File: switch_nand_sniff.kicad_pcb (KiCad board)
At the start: 2 copper layers, 35.4 x 28.8 mm, 3 parts, among them P1 CONN_02X15, P2 CONN_02X15

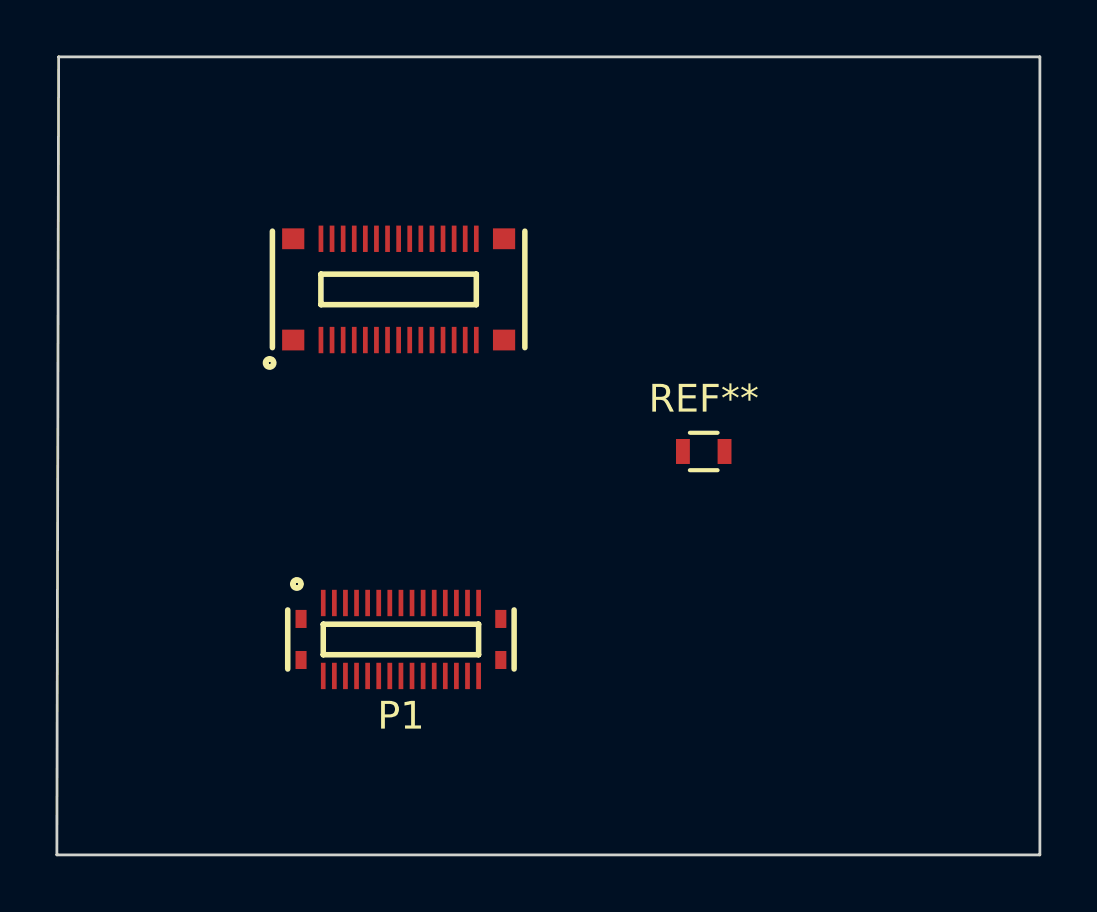
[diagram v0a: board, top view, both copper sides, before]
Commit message: Improved stencil design for manufacturing *removed resistor stencil because tbh why was it there in the first place *shrunk pad size to decrease risk of shorts when using solder paste *moved pads to edge of stencils to improve rate of manufacturing.
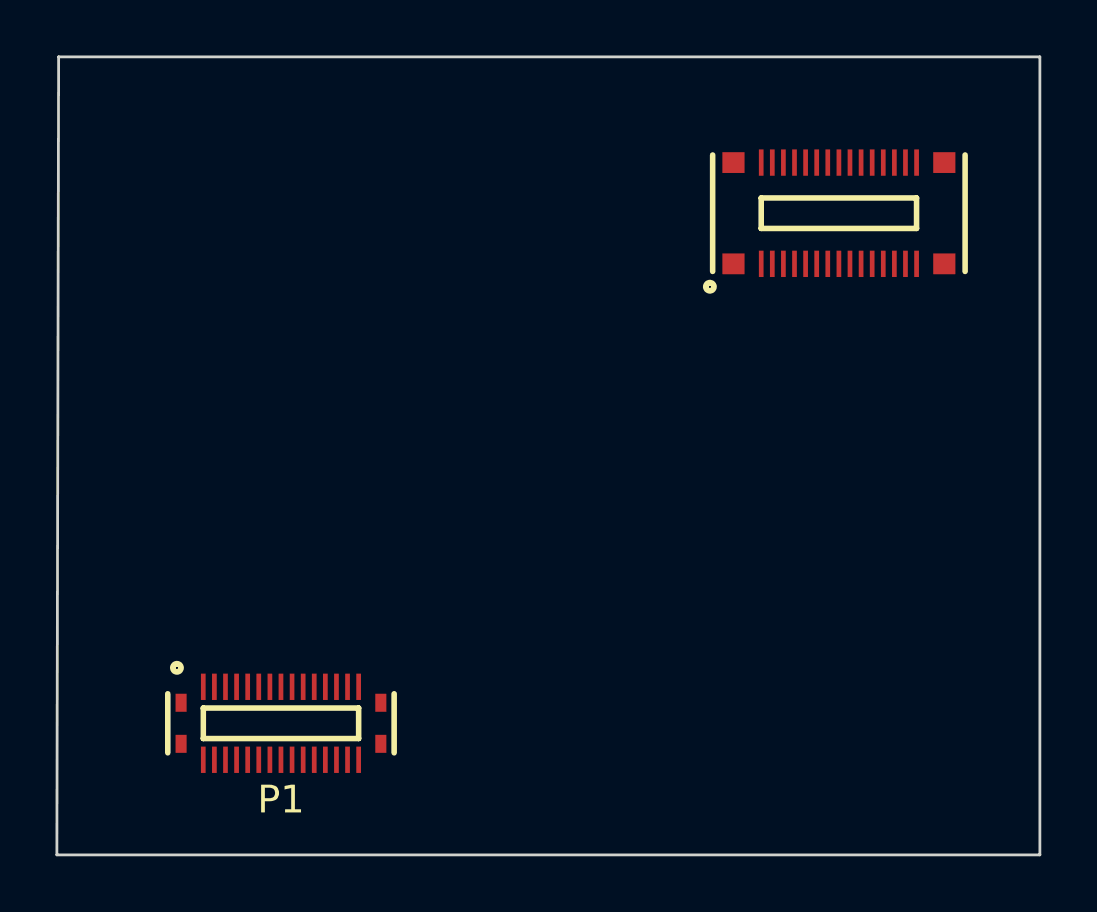
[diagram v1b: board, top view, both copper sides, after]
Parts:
- removed REF**: R_0603, Resistors_SMD:R_0603
- moved P2 16.1 mm to (152.8, 94.2)
- moved P1 5.28 mm to (132.7, 112.5)
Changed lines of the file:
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@@
     (tracks 0)
     (zones 0)
-    (modules 3)
+    (modules 2)
     (nets 1)
   )
@@
   )
   (module switch:55909-0374 (layer F.Cu)
-    (at 137.052 109.519)
+    (at 132.728 112.5405)
     (solder_mask_margin 0.035)
     (fp_text reference P1 (at 0 2.75) (layer F.SilkS)
@@
   )
   (module switch:500913-0302 (layer F.Cu)
-    (at 136.9695 96.901)
+    (at 152.8385 94.154)
     (solder_mask_margin 0.035)
     (fp_text reference P2 (at 0 3.4) (layer F.SilkS) hide
@@
     (pad 15 smd rect (at 2.8 1.825) (size 0.17 0.95) (layers F.Cu F.Paste F.Mask))
   )
-  (module Resistors_SMD:R_0603 (layer F.Cu)
-    (at 147.967 102.743)
-    (descr "Resistor SMD 0603, reflow soldering, Vishay (see dcrcw.pdf)")
-    (tags "resistor 0603")
-    (attr smd)
-    (fp_text reference REF** (at 0 -1.9) (layer F.SilkS)
-      (effects (font (size 1 1) (thickness 0.15)))
-    )
-    (fp_text value R_0603 (at 0 1.9) (layer F.Fab)
-      (effects (font (size 1 1) (thickness 0.15)))
-    )
-    (fp_line (start -1.3 -0.8) (end 1.3 -0.8) (layer F.CrtYd) (width 0.05))
-    (fp_line (start -1.3 0.8) (end 1.3 0.8) (layer F.CrtYd) (width 0.05))
-    (fp_line (start -1.3 -0.8) (end -1.3 0.8) (layer F.CrtYd) (width 0.05))
-    (fp_line (start 1.3 -0.8) (end 1.3 0.8) (layer F.CrtYd) (width 0.05))
-    (fp_line (start 0.5 0.675) (end -0.5 0.675) (layer F.SilkS) (width 0.15))
-    (fp_line (start -0.5 -0.675) (end 0.5 -0.675) (layer F.SilkS) (width 0.15))
-    (pad 1 smd rect (at -0.75 0) (size 0.5 0.9) (layers F.Cu F.Paste F.Mask))
-    (pad 2 smd rect (at 0.75 0) (size 0.5 0.9) (layers F.Cu F.Paste F.Mask))
-    (model Resistors_SMD.3dshapes/R_0603.wrl
-      (at (xyz 0 0 0))
-      (scale (xyz 1 1 1))
-      (rotate (xyz 0 0 0))
-    )
-  )
   (gr_line (start 124.6505 117.2845) (end 124.714 88.519) (layer Edge.Cuts) (width 0.1))
